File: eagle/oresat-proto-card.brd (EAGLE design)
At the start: 99.8 x 94.7 mm, 120 parts, among them J1 J-SAMTEC-TFM-110-X1-XXX-D-RA, J2 U.FL, J3 U.FL, J4 U.FL, J6 J-SAMTEC-TFM-120-X1-XXX-D-RA, J7 ORESAT-DEBUG-CONNECTOR-SOLAR, Q10 DMP2240UDM, Q2 MOSFET-PCH-SOT23-6, Q7 MOSFET-PCH-SOT23-6, Q8 PMV45EN, Q9 PMV45EN, U1 TCAN330, U10 TPS62111RSA, U11 MIC842LYC5, U12 MIC842LYC5, U2 MAX7310ATE, U6 MAX4211FETE, U7 STM32F091C, X2 16MHZ-2.5x2mm

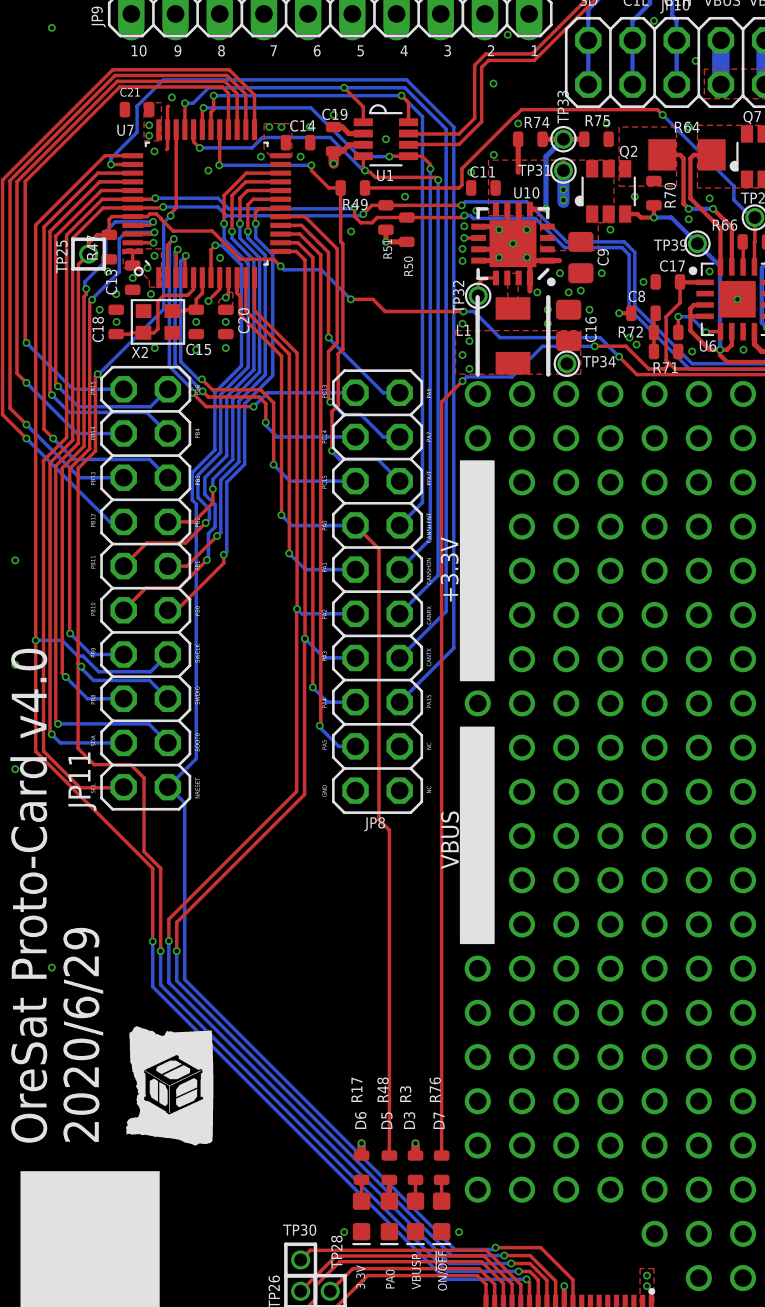
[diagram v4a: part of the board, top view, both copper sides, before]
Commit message: minor tweak to ground plane stitching
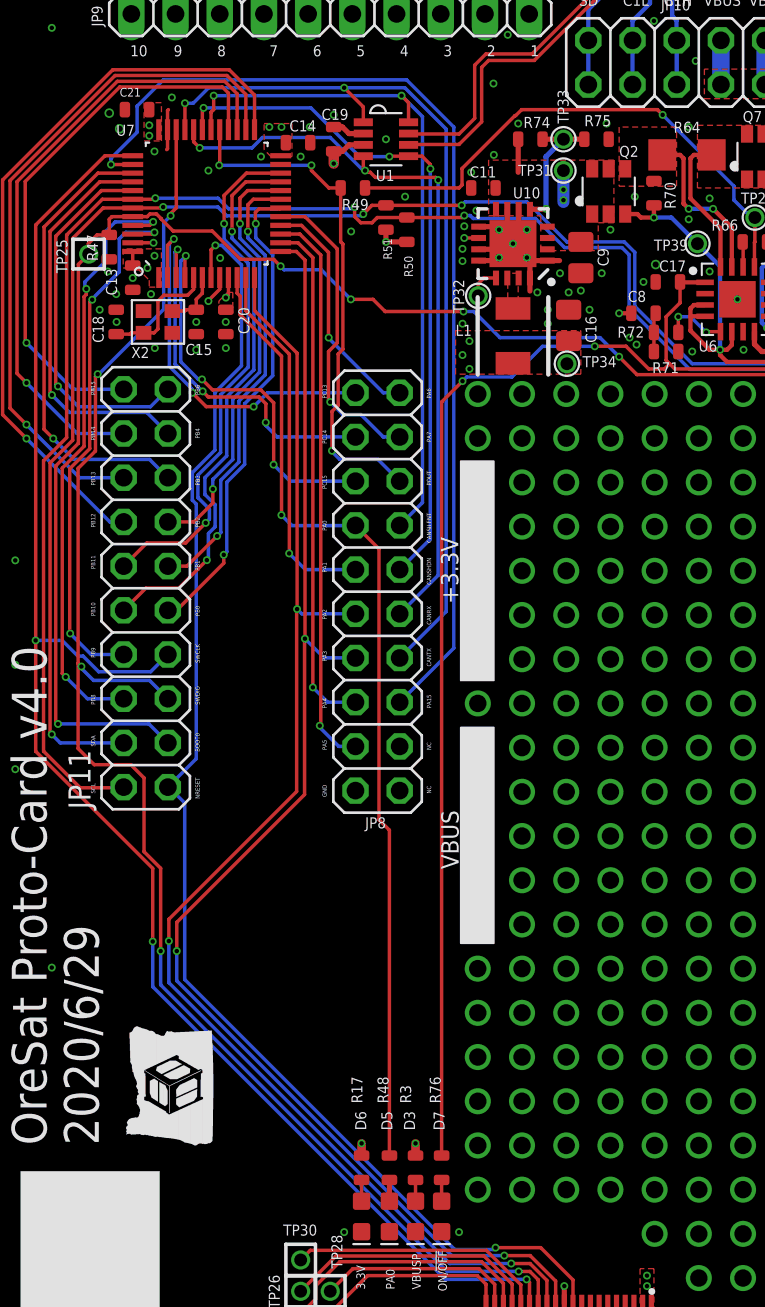
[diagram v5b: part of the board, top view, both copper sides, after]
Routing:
- net PA0: track 57.0 -> 56.2 mm
- net GND: vias 285 -> 288
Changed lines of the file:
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@@
 <layer number="27" name="tValues" color="7" fill="1" visible="no" active="yes"/>
 <layer number="28" name="bValues" color="7" fill="1" visible="no" active="yes"/>
-<layer number="29" name="tStop" color="7" fill="3" visible="no" active="yes"/>
+<layer number="29" name="tStop" color="7" fill="3" visible="yes" active="yes"/>
 <layer number="30" name="bStop" color="7" fill="6" visible="no" active="yes"/>
 <layer number="31" name="tCream" color="7" fill="4" visible="no" active="yes"/>
@@
 <contactref element="U7" pad="1"/>
 <wire x1="12.15" y1="67.65" x2="12.15" y2="68.1" width="0.1524" layer="1"/>
-<wire x1="10.65" y1="68.345" x2="10.695" y2="68.3" width="0.1524" layer="1"/>
 <contactref element="J7" pad="11"/>
 <via x="35.45" y="9.7" extent="1-16" drill="0.254"/>
@@
 <via x="39.2" y="64.2" extent="1-16" drill="0.254"/>
 <wire x1="11.845" y1="69.65" x2="10.65" y2="69.65" width="0.2" layer="1"/>
-<wire x1="15.65" y1="66.978975" x2="15.1855125" y2="66.5144875" width="0.2" layer="1"/>
+<wire x1="15.65" y1="66.978975" x2="15" y2="66.328975" width="0.2" layer="1"/>
 <wire x1="15.65" y1="67.65" x2="15.65" y2="66.978975" width="0.2" layer="1"/>
 <via x="15" y="66.3" extent="1-16" drill="0.254"/>
@@
 <wire x1="12.65" y1="76.15" x2="12.65" y2="75.05" width="0.2" layer="1"/>
 <wire x1="12.65" y1="75.05" x2="12.6" y2="75" width="0.2" layer="1"/>
-<wire x1="12.65" y1="76.15" x2="12.65" y2="77.45" width="0.2" layer="1"/>
-<wire x1="12.65" y1="77.45" x2="12.7" y2="77.5" width="0.2" layer="1"/>
+<wire x1="12.65" y1="76.15" x2="12.65" y2="77.25" width="0.2" layer="1"/>
+<wire x1="12.65" y1="77.25" x2="12.7" y2="77.3" width="0.2" layer="1"/>
 <via x="12.9" y="78" extent="1-16" drill="0.254"/>
 <via x="8.75" y="65.8" extent="1-16" drill="0.254"/>
 <via x="73.9" y="76.2" extent="1-16" drill="0.254"/>
-<wire x1="85.678" y1="85.62" x2="85.932" y2="88.922" width="0" layer="19" extent="1-16"/>
-<wire x1="85.25" y1="83.875" x2="85.678" y2="85.62" width="0" layer="19" extent="1-1"/>
-<wire x1="15.1855125" y1="66.5144875" x2="15" y2="66.3" width="0" layer="19" extent="1-1"/>
-<wire x1="12.7" y1="77.5" x2="12.9" y2="78" width="0" layer="19" extent="1-1"/>
-<wire x1="73.9" y1="75.3" x2="74.6" y2="75.3" width="0" layer="19" extent="1-1"/>
-<wire x1="72.1" y1="67.7" x2="72.1" y2="67" width="0" layer="19" extent="1-1"/>
-<wire x1="73.2" y1="68.2" x2="73.2" y2="67.5" width="0" layer="19" extent="1-1"/>
-<wire x1="61.2" y1="76.1" x2="61.9" y2="76.1" width="0" layer="19" extent="1-1"/>
-<wire x1="56.8" y1="76.1" x2="57.5" y2="76.1" width="0" layer="19" extent="1-1"/>
-<wire x1="52.4" y1="76.1" x2="51.7" y2="76.1" width="0" layer="19" extent="1-1"/>
-<wire x1="53.1" y1="73.1" x2="53.1" y2="73.8" width="0" layer="19" extent="1-1"/>
-<wire x1="55.3" y1="70.1" x2="56" y2="70.1" width="0" layer="19" extent="1-1"/>
-<wire x1="49.9" y1="65.8" x2="50.6" y2="65.8" width="0" layer="19" extent="1-1"/>
-<wire x1="40.7" y1="67.4" x2="40" y2="67.4" width="0" layer="19" extent="1-1"/>
-<wire x1="22.2" y1="76.3" x2="22.2" y2="77" width="0" layer="19" extent="1-1"/>
-<wire x1="16" y1="64.4" x2="15.995" y2="65.1" width="0" layer="19" extent="1-1"/>
-<wire x1="14.3" y1="64.4" x2="14.3" y2="65.1" width="0" layer="19" extent="1-1"/>
-<wire x1="9.3" y1="68.7" x2="9.22" y2="68" width="0" layer="19" extent="1-1"/>
-<wire x1="9.7" y1="65.8" x2="9.72" y2="65.1" width="0" layer="19" extent="1-1"/>
-<wire x1="54.3525" y1="66.157" x2="55.15" y2="66.15" width="0" layer="19" extent="1-1"/>
-<wire x1="42" y1="63.4" x2="42.8" y2="63.4" width="0" layer="19" extent="1-1"/>
-<wire x1="74.05" y1="73.4" x2="73.2" y2="73.4" width="0" layer="19" extent="1-1"/>
-<wire x1="70.4" y1="67.55" x2="70.4" y2="68.4" width="0" layer="19" extent="1-1"/>
-<wire x1="62.1" y1="67.5" x2="63" y2="67.5" width="0" layer="19" extent="1-1"/>
-<wire x1="49.9" y1="67" x2="49.9" y2="67.9" width="0" layer="19" extent="1-1"/>
-<wire x1="38" y1="75.6" x2="37.88" y2="76.5" width="0" layer="19" extent="1-1"/>
-<wire x1="30.1" y1="72.8" x2="30.1" y2="73.7" width="0" layer="19" extent="1-1"/>
-<wire x1="20.85" y1="75.4" x2="20.825" y2="76.3" width="0" layer="19" extent="1-1"/>
-<wire x1="56.9404" y1="69.525" x2="56" y2="69.4" width="0" layer="19" extent="1-1"/>
-<wire x1="51.943" y1="73.5525" x2="52" y2="72.6" width="0" layer="19" extent="1-1"/>
-<wire x1="79.275" y1="82.2" x2="80.25" y2="82.175" width="0" layer="19" extent="1-1"/>
-<wire x1="10.65" y1="66.945" x2="9.7" y2="66.7" width="0" layer="19" extent="1-1"/>
-<wire x1="85.275" y1="82.2" x2="86.275" y2="82.175" width="0" layer="19" extent="1-1"/>
-<wire x1="65.2" y1="68.4" x2="65" y2="67.4" width="0" layer="19" extent="1-1"/>
-<wire x1="36.4" y1="67.9" x2="36.4" y2="66.9" width="0" layer="19" extent="1-1"/>
-<wire x1="35.7" y1="65.8" x2="35.7" y2="66.8" width="0" layer="19" extent="1-1"/>
-<wire x1="28.4" y1="12.823" x2="29.4" y2="12.8" width="0" layer="19" extent="1-1"/>
-<wire x1="23.8" y1="12.823" x2="22.8" y2="12.8" width="0" layer="19" extent="1-1"/>
-<wire x1="45.725" y1="64.5404" x2="45.75" y2="63.5" width="0" layer="19" extent="1-1"/>
-<wire x1="76.525" y1="82.2" x2="75.475" y2="82.225" width="0" layer="19" extent="1-1"/>
-<wire x1="73.275" y1="82.2" x2="74.325" y2="82.2" width="0" layer="19" extent="1-1"/>
-<wire x1="11.275" y1="65.725" x2="11.7" y2="66.7" width="0" layer="19" extent="1-1"/>
-<wire x1="82.525" y1="82.2" x2="81.425" y2="82.2" width="0" layer="19" extent="1-1"/>
-<wire x1="70.525" y1="82.2" x2="69.45" y2="82.175" width="0" layer="19" extent="1-1"/>
-<wire x1="36.45" y1="8.7" x2="36.5" y2="7.5" width="0" layer="19" extent="1-1"/>
-<wire x1="37.95" y1="8.7" x2="38" y2="7.5" width="0" layer="19" extent="1-1"/>
-<wire x1="28.7" y1="6.8" x2="27.5" y2="6.8" width="0" layer="19" extent="1-1"/>
-<wire x1="19.15" y1="74.15" x2="18.02" y2="74.6" width="0" layer="19" extent="1-1"/>
-<wire x1="42.7" y1="6.8" x2="41.4" y2="6.8" width="0" layer="19" extent="1-1"/>
-<wire x1="12.925" y1="64.475" x2="11.92" y2="63.6" width="0" layer="19" extent="1-1"/>
-<wire x1="26.9" y1="12.823" x2="28.4" y2="12.823" width="0" layer="19" extent="1-1"/>
-<wire x1="25.4" y1="12.823" x2="26.9" y2="12.823" width="0" layer="19" extent="1-1"/>
-<wire x1="82.122" y1="85.62" x2="82.55" y2="83.9" width="0" layer="19" extent="1-1"/>
-<wire x1="79.678" y1="85.62" x2="79.275" y2="83.9" width="0" layer="19" extent="1-1"/>
-<wire x1="73.678" y1="85.62" x2="73.275" y2="83.875" width="0" layer="19" extent="1-1"/>
-<wire x1="70.122" y1="85.62" x2="70.525" y2="83.9" width="0" layer="19" extent="1-1"/>
-<wire x1="76.122" y1="85.62" x2="76.525" y2="83.85" width="0" layer="19" extent="1-1"/>
-<wire x1="10.2" y1="77.3" x2="12.7" y2="77.5" width="0" layer="19" extent="1-1"/>
-<wire x1="81.868" y1="88.922" x2="82.122" y2="85.62" width="0" layer="19" extent="1-16"/>
-<wire x1="79.932" y1="88.922" x2="81.868" y2="88.922" width="0" layer="19" extent="16-16"/>
-<wire x1="73.932" y1="88.922" x2="73.678" y2="85.62" width="0" layer="19" extent="1-16"/>
-<wire x1="75.868" y1="88.922" x2="73.932" y2="88.922" width="0" layer="19" extent="16-16"/>
-<wire x1="69.868" y1="88.922" x2="70.122" y2="85.62" width="0" layer="19" extent="1-16"/>
+<via x="40.7" y="68.4" extent="1-16" drill="0.35"/>
+<via x="9.3" y="77.1" extent="1-16" drill="0.35"/>
+<via x="9.9" y="76.2" extent="1-16" drill="0.35"/>
+<wire x1="15" y1="66.3" x2="15" y2="66.328975" width="0.2" layer="1"/>
 </signal>
 <signal name="BOOT0">
@@
 </signal>
 <signal name="PA8/POUTPROT">
-<wire x1="15.6" y1="74.12" x2="15.62" y2="74.1" width="0.2" layer="1"/>
 <via x="15.62" y="74.1" extent="1-16" drill="0.254"/>
 <via x="20.92" y="74.1" extent="1-16" drill="0.254"/>
@@
 <contactref element="R48" pad="2"/>
 <contactref element="JP8" pad="7"/>
-<wire x1="16.65" y1="67.65" x2="16.65" y2="66.85" width="0.2" layer="1"/>
-<wire x1="16.65" y1="67.65" x2="16.65" y2="66.75" width="0.2" layer="1"/>
 <wire x1="16.823" y1="66.577" x2="16.823" y2="65.51455" width="0.2" layer="1"/>
 <via x="19.1944" y="54" extent="1-16" drill="0.254"/>
@@
 <wire x1="23.44" y1="53.4" x2="19.7944" y2="53.4" width="0.2" layer="16"/>
 <wire x1="19.1944" y1="54" x2="19.7944" y2="53.4" width="0.2" layer="16"/>
-<wire x1="16.65" y1="66.75" x2="16.823" y2="66.577" width="0.2" layer="1"/>
+<wire x1="16.823" y1="66.577" x2="16.65" y2="66.75" width="0.2" layer="1"/>
 <wire x1="16.823" y1="65.51455" x2="19.2" y2="63.13755" width="0.2" layer="1"/>
 <wire x1="19.1944" y1="54" x2="19.2" y2="54.0056" width="0.2" layer="1"/>
@@
 <wire x1="24.8" y1="36.5" x2="24.8" y2="52.06" width="0.2" layer="1"/>
 <wire x1="25.4" y1="35.9" x2="24.8" y2="36.5" width="0.2" layer="1"/>
+<wire x1="16.65" y1="66.75" x2="16.65" y2="67.65" width="0.2" layer="1"/>
 </signal>
 <signal name="PA4">
@@
 <contactref element="JP11" pad="15"/>
 <wire x1="10.65" y1="73.65" x2="8.65" y2="73.65" width="0.2" layer="1"/>
-<wire x1="12.6286625" y1="56.15" x2="12.67" y2="56.15" width="0.2" layer="1"/>
 <wire x1="8.65" y1="73.65" x2="5.554" y2="70.554" width="0.2" layer="1"/>
 <wire x1="5.554" y1="58.9286" x2="6.0826" y2="58.4" width="0.2" layer="1"/>
@@
 <wire x1="16.3556" y1="72.364175" x2="16.3556" y2="70.3" width="0.2" layer="1"/>
 <wire x1="14.8" y1="56.15568125" x2="14.8" y2="55.1842" width="0.2" layer="16"/>
-<wire x1="10.1713375" y1="48.53" x2="10.13" y2="48.53" width="0.2" layer="16"/>
 <wire x1="16.3556" y1="69.9" x2="17.6128" y2="68.6428" width="0.2" layer="16"/>
 <wire x1="17.6128" y1="68.6428" x2="17.6128" y2="62.35" width="0.2" layer="16"/>
@@
 <contactref element="D6" pad="A"/>
 <contactref element="R17" pad="1"/>
-<wire x1="23.8" y1="14.577" x2="23.7" y2="14.677" width="0.2" layer="1"/>
 <wire x1="23.8" y1="15.8" x2="23.8" y2="14.577" width="0.2" layer="1"/>
 </signal>

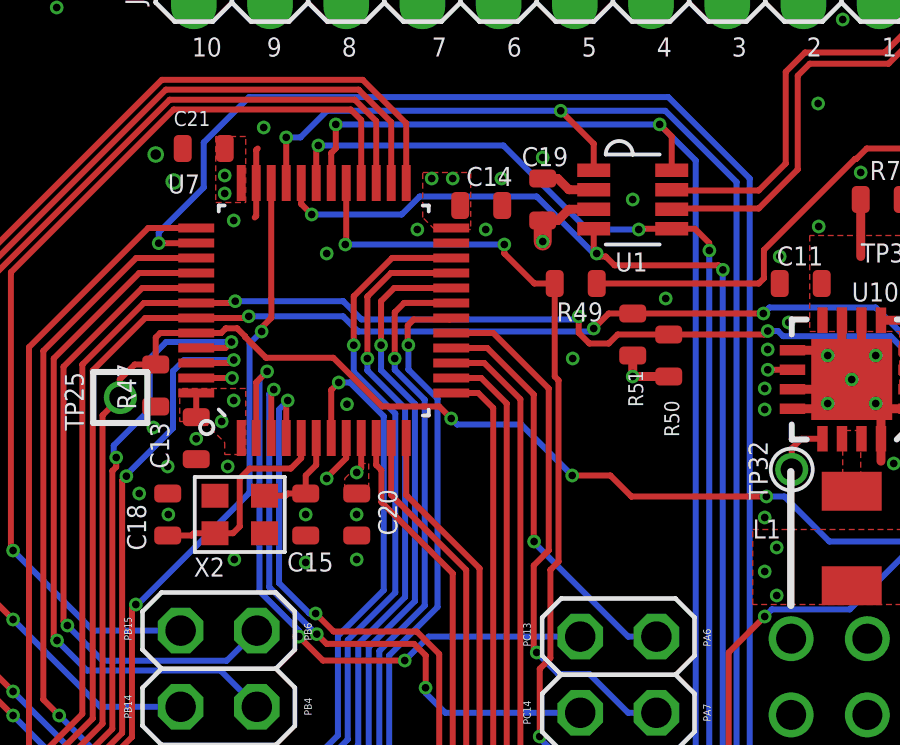
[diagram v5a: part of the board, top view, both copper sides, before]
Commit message: fixed an error where Pout was not routed to an ADC pin
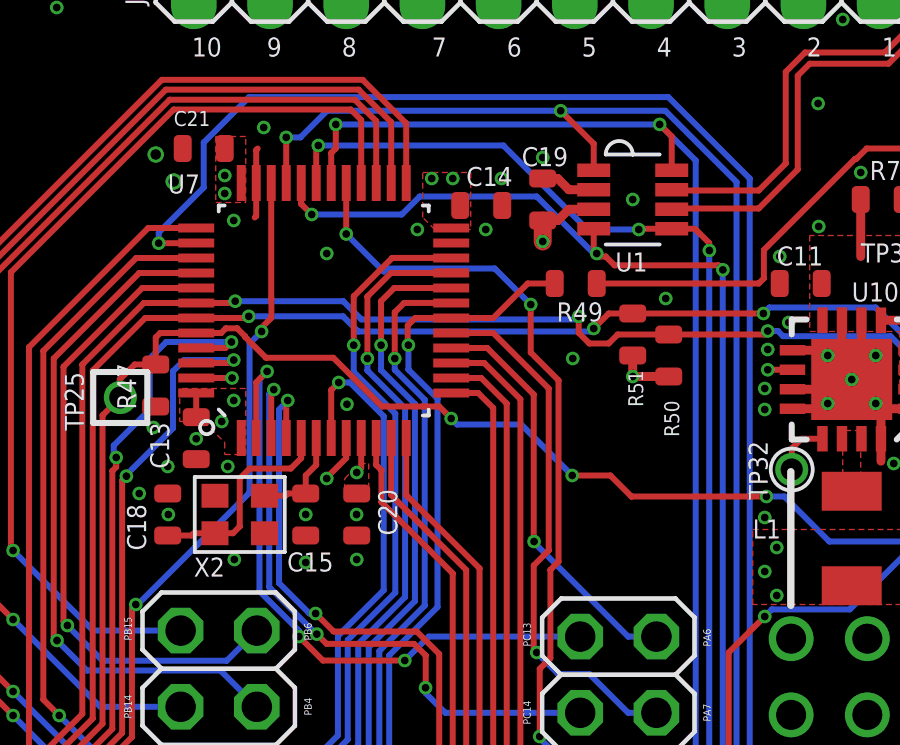
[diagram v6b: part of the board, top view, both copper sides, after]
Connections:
- removed net PA8/POUTPROT: JP8.6, R49.2, U7.29
- removed net PB0: JP11.9, U7.18
- new net PA8: JP8.6, U7.29
- new net PB0/POUTPROT: JP11.9, R49.2, U7.18
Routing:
- net PB0/POUTPROT: track 0.00 -> 31.5 mm, vias 0 -> 2
- net PA8/POUTPROT: track 29.8 -> 0.00 mm, vias 3 -> 0
- net PA8: track 0.00 -> 28.6 mm, vias 0 -> 3
- net PB0: track 27.6 -> 0.00 mm, vias 2 -> 0

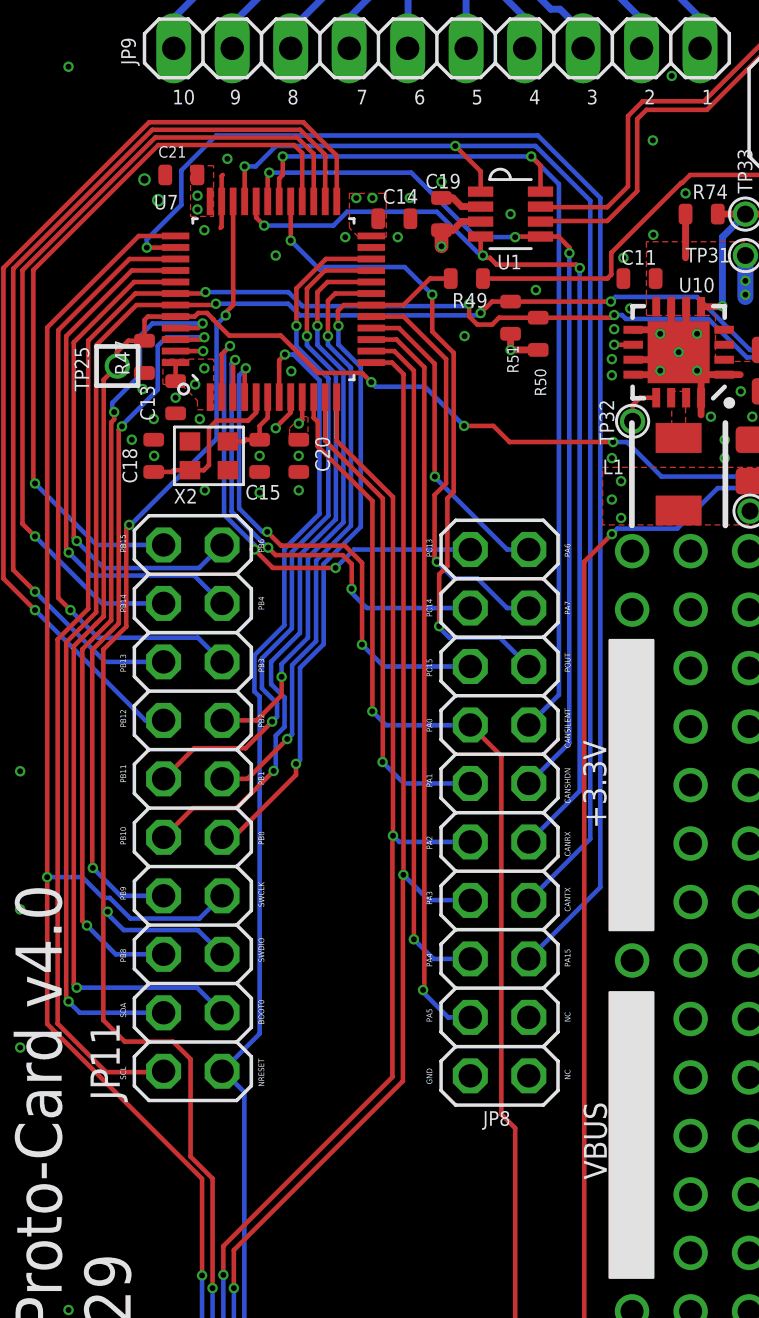
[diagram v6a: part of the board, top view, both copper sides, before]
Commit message: Minor DRC clean up, fixed 3.3V plane cut by VBUSP, and some TSTOPs being too close.
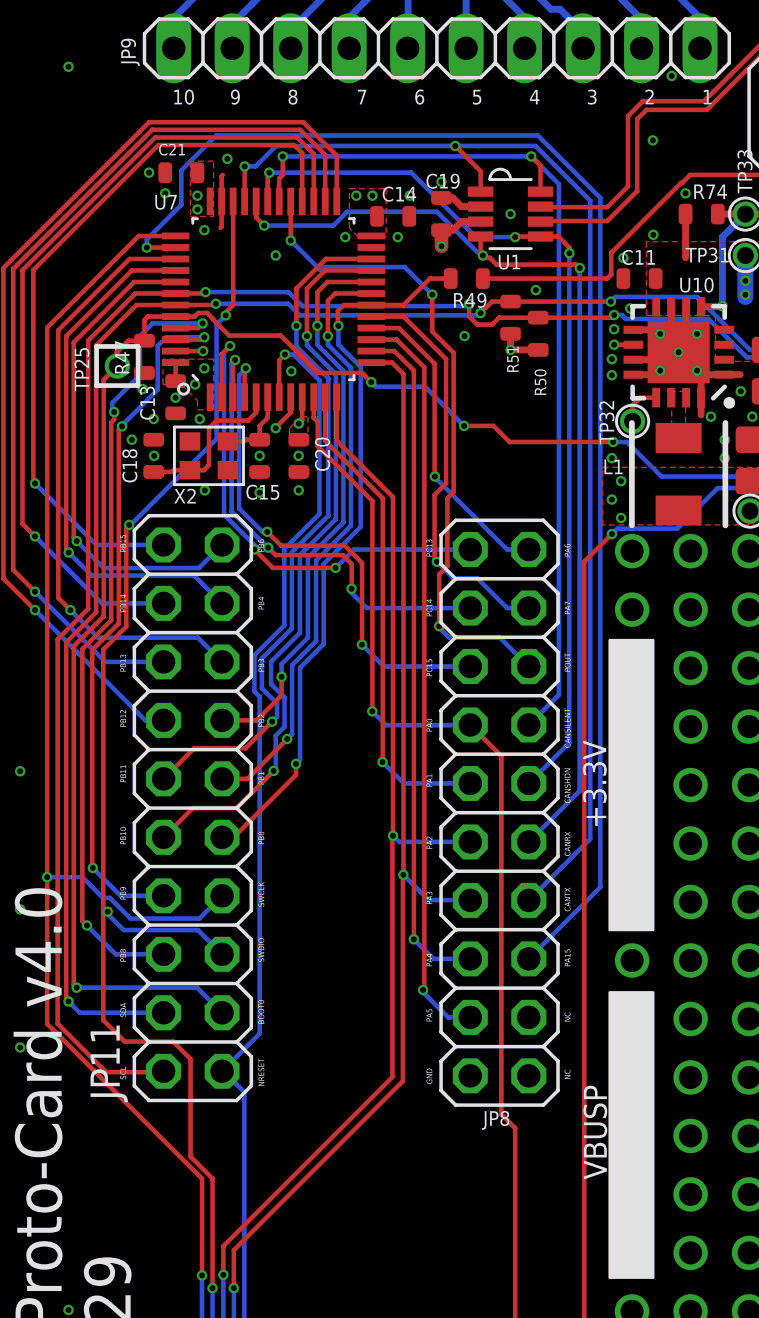
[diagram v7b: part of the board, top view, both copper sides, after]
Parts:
- moved C14 0.11 mm to (20.1, 75.5)
- moved C21 0.10 mm to (10.9, 77.4)
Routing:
- net VBUSP: track 108.7 -> 38.4 mm
- added copper zone on layer 15, net VBUSP
